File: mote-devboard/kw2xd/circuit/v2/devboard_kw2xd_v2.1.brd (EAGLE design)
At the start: 41.6 x 55.9 mm, 21 parts, among them J1 CORTEX_DEBUG_PTH, Q1 RED, Q2 RED, Q3 GREEN

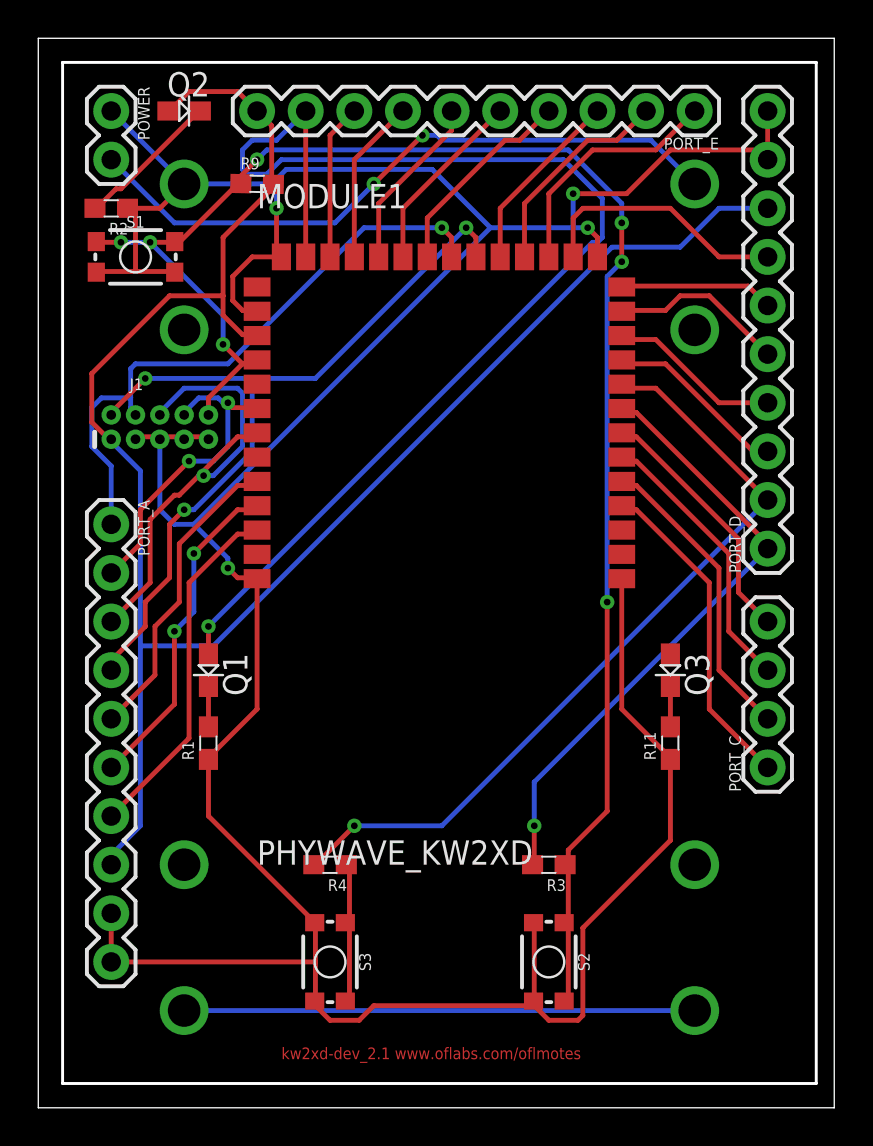
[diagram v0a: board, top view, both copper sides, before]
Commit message: Changed cpu mode to FEI so we don't rely on radio clock Minor changes in board design
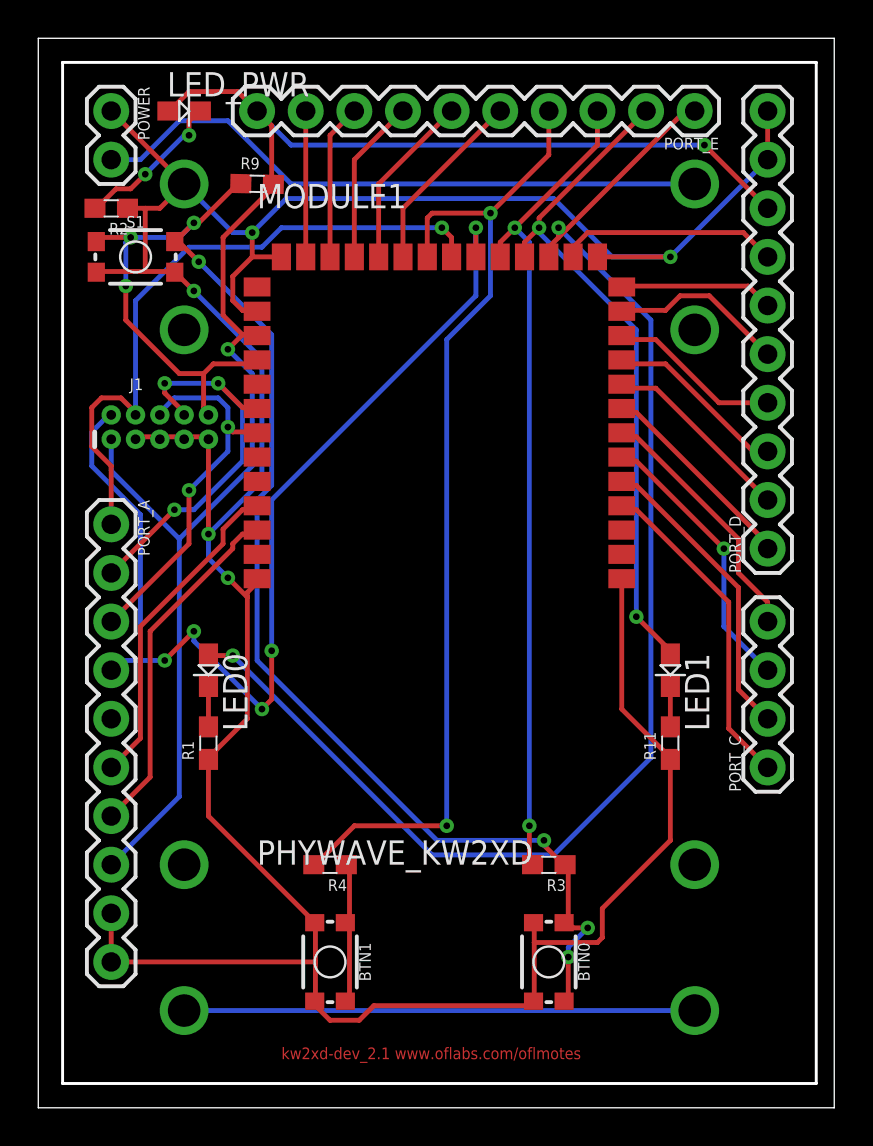
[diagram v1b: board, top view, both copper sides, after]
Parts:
- LED_PWR: value RED -> ORANGE
- renumbered Q1 to LED0, Q2 to LED_PWR, Q3 to LED1, S2 to BTN0, S3 to BTN1
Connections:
- net PTD1: no longer R3.2
- net PTD2: no longer R4.2
- net PTE0: now also LED0.A
- net PTE1: now also LED1.A
- net PTE18: no longer LED1.A
- net PTE19: no longer LED0.A
- net PTE2: now also R3.2
- net PTE3: now also R4.2
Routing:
- net PTE0: track 12.7 -> 70.9 mm, vias 0 -> 2
- net PTE19: track 65.3 -> 7.62 mm, vias 1 -> 0
- net PTE3: track 10.7 -> 52.8 mm, vias 0 -> 2
- net PTE2: track 9.72 -> 43.5 mm, vias 0 -> 2
- net PTD2: track 41.8 -> 10.2 mm, vias 1 -> 0
- net PTE1: track 11.1 -> 35.4 mm, vias 0 -> 2
- net PTD1: track 32.6 -> 10.9 mm, vias 1 -> 0
- net PTA4: track 16.2 -> 0.00 mm
- net PTA3_SWDIO: track 43.0 -> 56.4 mm, vias 3 -> 5
- net GND: track 186.9 -> 175.6 mm, vias 4 -> 5
- net VCC: track 98.1 -> 86.9 mm, vias 0 -> 2
- net NRST: track 87.2 -> 79.5 mm
- net PTA2_SWO: track 24.5 -> 19.6 mm, vias 1 -> 2
- net PTA1_TDI: track 16.7 -> 21.3 mm, vias 2 -> 3
- net PTA0_SWDCLK: track 32.3 -> 34.7 mm
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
